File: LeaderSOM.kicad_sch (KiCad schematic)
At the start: 0 parts

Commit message: driver controls + lighting architecture
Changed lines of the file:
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@@
 (kicad_sch
-	(version 20231120)
+	(version 20250114)
 	(generator "eeschema")
-	(generator_version "8.0")
+	(generator_version "9.0")
 	(paper "A4")
-	(hierarchical_label "+5V_CarCAN"
+	(hierarchical_label "+12V_CarCAN"
 		(shape input)
 		(at 53.34 71.755 0)
-		(fields_autoplaced yes)
 		(effects
 			(font
@@
 		(shape input)
 		(at 53.34 62.865 0)
-		(fields_autoplaced yes)
 		(effects
 			(font
@@
 		(shape output)
 		(at 53.34 95.885 0)
-		(fields_autoplaced yes)
 		(effects
 			(font
@@
 		(shape input)
 		(at 53.34 81.28 0)
-		(fields_autoplaced yes)
 		(effects
 			(font
@@
 		(shape output)
 		(at 53.34 105.41 0)
-		(fields_autoplaced yes)
 		(effects
 			(font
@@
 		(shape input)
 		(at 53.34 75.565 0)
-		(fields_autoplaced yes)
 		(effects
 			(font
@@
 		(shape input)
 		(at 53.34 58.42 0)
-		(fields_autoplaced yes)
 		(effects
 			(font
@@
 		(shape input)
 		(at 53.34 85.09 0)
-		(fields_autoplaced yes)
 		(effects
 			(font
@@
 		(shape output)
 		(at 53.34 101.6 0)
-		(fields_autoplaced yes)
 		(effects
 			(font
@@
 		(shape output)
 		(at 53.34 92.075 0)
-		(fields_autoplaced yes)
 		(effects
 			(font

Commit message: bye
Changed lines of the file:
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@@
 	(generator_version "9.0")
 	(paper "A4")
-	(hierarchical_label "+12V_CarCAN"
-		(shape input)
-		(at 53.34 71.755 0)
-		(effects
-			(font
-				(size 1.27 1.27)
-			)
-			(justify left)
-		)
-	)
 	(hierarchical_label "GND"
 		(shape input)
@@
 		(effects
 			(font
-				(size 1.27 1.27)
-			)
-			(justify left)
-		)
-	)
-	(hierarchical_label "GND_CarCAN"
-		(shape input)
-		(at 53.34 75.565 0)
-		(effects
-			(font

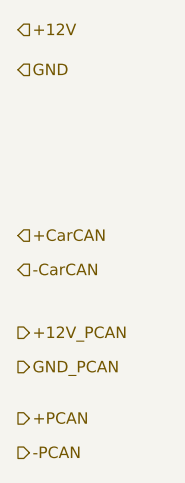
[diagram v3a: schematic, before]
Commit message: Updated Controls + Telemetry
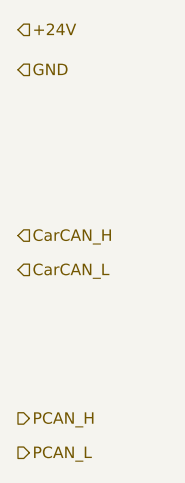
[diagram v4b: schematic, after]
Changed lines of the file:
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@@
 		)
 	)
-	(hierarchical_label "GND_PCAN"
-		(shape output)
-		(at 53.34 95.885 0)
-		(effects
-			(font
-				(size 1.27 1.27)
-			)
-			(justify left)
-		)
-	)
-	(hierarchical_label "+CarCAN"
+	(hierarchical_label "CarCAN_H"
 		(shape input)
 		(at 53.34 81.28 0)
@@
 		)
 	)
-	(hierarchical_label "-PCAN"
+	(hierarchical_label "PCAN_L"
 		(shape output)
 		(at 53.34 105.41 0)
@@
 		)
 	)
-	(hierarchical_label "+12V"
+	(hierarchical_label "+24V"
 		(shape input)
 		(at 53.34 58.42 0)
@@
 		)
 	)
-	(hierarchical_label "-CarCAN"
+	(hierarchical_label "CarCAN_L"
 		(shape input)
 		(at 53.34 85.09 0)
@@
 		)
 	)
-	(hierarchical_label "+PCAN"
+	(hierarchical_label "PCAN_H"
 		(shape output)
 		(at 53.34 101.6 0)
 		(effects
 			(font
-				(size 1.27 1.27)
-			)
-			(justify left)
-		)
-	)
-	(hierarchical_label "+12V_PCAN"
-		(shape output)
-		(at 53.34 92.075 0)
-		(effects
-			(font
